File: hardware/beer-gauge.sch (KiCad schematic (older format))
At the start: 32 parts, among them J1 OLED_MODULE, P1 CONN_01X04, P2 CONN_01X04, P3 CONN_01X04, P4 CONN_01X04, U1 ADS1232IPW, U5 TCA9543A, U6 SN74LVC1G58

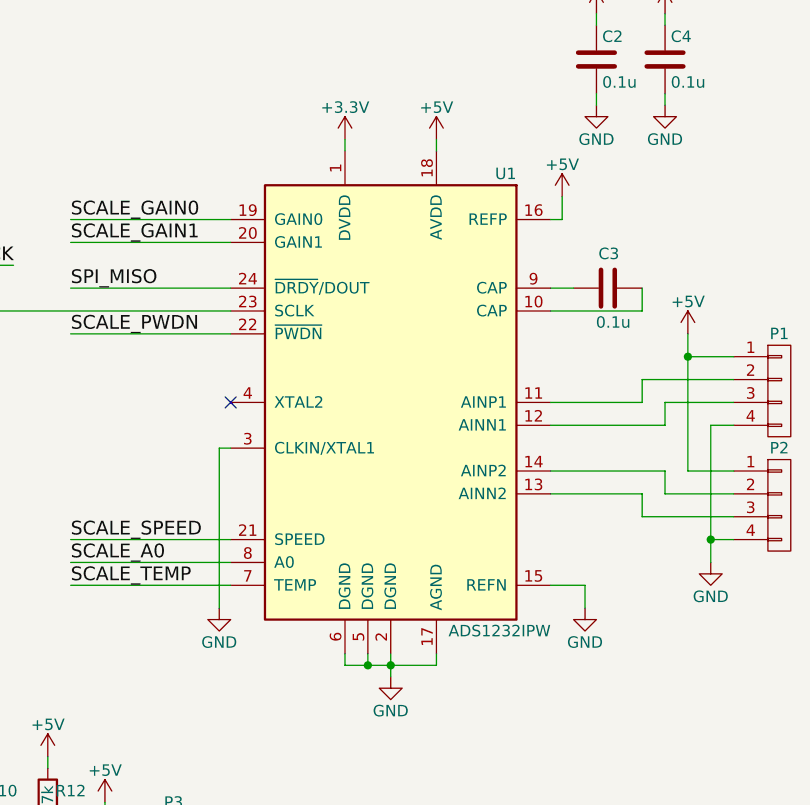
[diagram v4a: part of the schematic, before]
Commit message: Updating layout with schematic changes
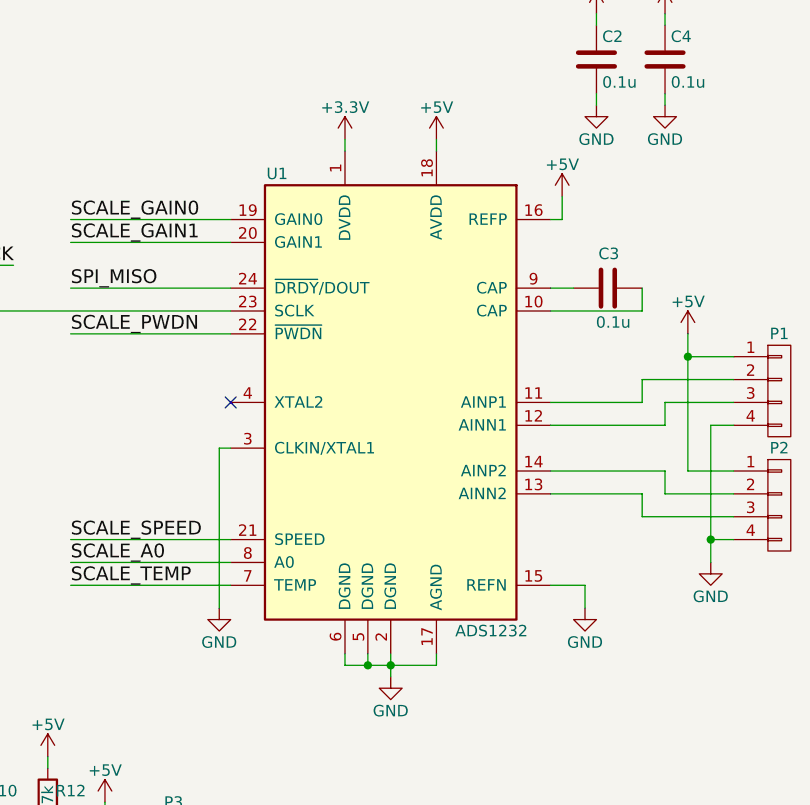
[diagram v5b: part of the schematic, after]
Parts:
- U1: value ADS1232IPW -> ADS1232
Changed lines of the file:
@@
 U 1 1 577FD904
 P 8100 2750
-F 0 "U1" H 7550 3750 50  0000 L CNN
-F 1 "ADS1232IPW" H 7400 1750 50  0000 L CNN
+F 0 "U1" H 8550 3750 50  0000 L CNN
+F 1 "ADS1232" H 7500 1750 50  0000 L CNN
 F 2 "Housings_SSOP:TSSOP-24_4.4x7.8mm_Pitch0.65mm" H 8100 2750 50  0001 C CIN
 F 3 "" H 8100 2750 50  0000 C CNN

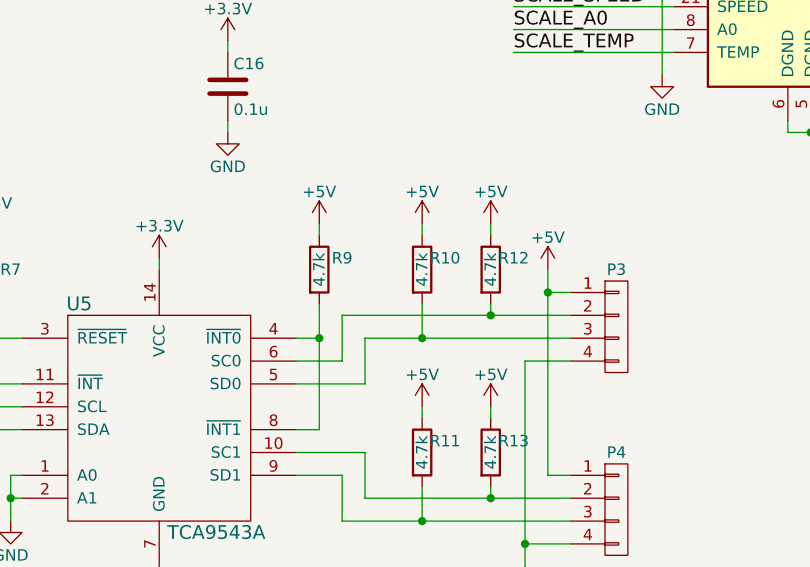
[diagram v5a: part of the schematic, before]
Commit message: Finished layout of traces
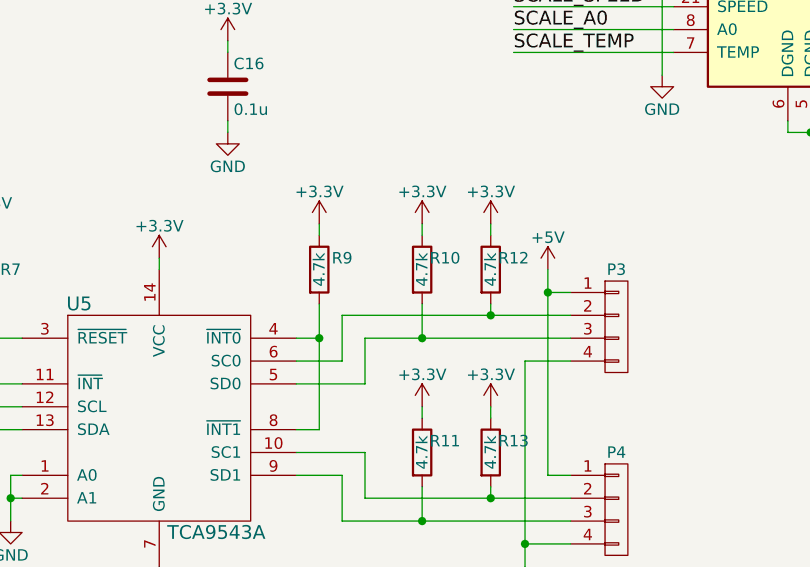
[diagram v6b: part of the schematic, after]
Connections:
- net +3V3: now also R10.1, R11.1, R12.1, R13.1, R9.1
- net +5V: no longer R10.1, R11.1, R12.1, R13.1, R9.1
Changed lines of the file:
@@
 	5750 4800 5850 4800
 Connection ~ 5850 4800
-$Comp
-L +5V #PWR033
-U 1 1 578242EC
-P 5850 4300
-F 0 "#PWR033" H 5850 4150 50  0001 C CNN
-F 1 "+5V" H 5850 4440 50  0000 C CNN
-F 2 "" H 5850 4300 50  0000 C CNN
-F 3 "" H 5850 4300 50  0000 C CNN
-	1    5850 4300
-	1    0    0    -1
-$EndComp
 Wire Wire Line
 	5850 4300 5850 4350
@@
 	6300 5450 6300 5600
 Connection ~ 6300 5600
-$Comp
-L +5V #PWR034
-U 1 1 57824D40
-P 6300 4300
-F 0 "#PWR034" H 6300 4150 50  0001 C CNN
-F 1 "+5V" H 6300 4440 50  0000 C CNN
-F 2 "" H 6300 4300 50  0000 C CNN
-F 3 "" H 6300 4300 50  0000 C CNN
-	1    6300 4300
-	1    0    0    -1
-$EndComp
-$Comp
-L +5V #PWR035
-U 1 1 57824E9B
-P 6600 4300
-F 0 "#PWR035" H 6600 4150 50  0001 C CNN
-F 1 "+5V" H 6600 4440 50  0000 C CNN
-F 2 "" H 6600 4300 50  0000 C CNN
-F 3 "" H 6600 4300 50  0000 C CNN
-	1    6600 4300
-	1    0    0    -1
-$EndComp
-$Comp
-L +5V #PWR036
-U 1 1 57824FF6
-P 6300 5100
-F 0 "#PWR036" H 6300 4950 50  0001 C CNN
-F 1 "+5V" H 6300 5240 50  0000 C CNN
-F 2 "" H 6300 5100 50  0000 C CNN
-F 3 "" H 6300 5100 50  0000 C CNN
-	1    6300 5100
-	1    0    0    -1
-$EndComp
-$Comp
-L +5V #PWR037
-U 1 1 57825151
-P 6600 5100
-F 0 "#PWR037" H 6600 4950 50  0001 C CNN
-F 1 "+5V" H 6600 5240 50  0000 C CNN
-F 2 "" H 6600 5100 50  0000 C CNN
-F 3 "" H 6600 5100 50  0000 C CNN
-	1    6600 5100
-	1    0    0    -1
-$EndComp
 Wire Wire Line
 	6600 5100 6600 5150
@@
 Wire Wire Line
 	6600 4300 6600 4350
+$Comp
+L +3.3V #PWR?
+U 1 1 577D9D9F
+P 5850 4300
+F 0 "#PWR?" H 5850 4150 50  0001 C CNN
+F 1 "+3.3V" H 5850 4440 50  0000 C CNN
+F 2 "" H 5850 4300 50  0000 C CNN
+F 3 "" H 5850 4300 50  0000 C CNN
+	1    5850 4300
+	1    0    0    -1
+$EndComp
+$Comp
+L +3.3V #PWR?
+U 1 1 577D9EFA
+P 6300 4300
+F 0 "#PWR?" H 6300 4150 50  0001 C CNN
+F 1 "+3.3V" H 6300 4440 50  0000 C CNN
+F 2 "" H 6300 4300 50  0000 C CNN
+F 3 "" H 6300 4300 50  0000 C CNN
+	1    6300 4300
+	1    0    0    -1
+$EndComp
+$Comp
+L +3.3V #PWR?
+U 1 1 577DA055
+P 6600 4300
+F 0 "#PWR?" H 6600 4150 50  0001 C CNN
+F 1 "+3.3V" H 6600 4440 50  0000 C CNN
+F 2 "" H 6600 4300 50  0000 C CNN
+F 3 "" H 6600 4300 50  0000 C CNN
+	1    6600 4300
+	1    0    0    -1
+$EndComp
+$Comp
+L +3.3V #PWR?
+U 1 1 577DA711
+P 6300 5100
+F 0 "#PWR?" H 6300 4950 50  0001 C CNN
+F 1 "+3.3V" H 6300 5240 50  0000 C CNN
+F 2 "" H 6300 5100 50  0000 C CNN
+F 3 "" H 6300 5100 50  0000 C CNN
+	1    6300 5100
+	1    0    0    -1
+$EndComp
+$Comp
+L +3.3V #PWR?
+U 1 1 577DA86C
+P 6600 5100
+F 0 "#PWR?" H 6600 4950 50  0001 C CNN
+F 1 "+3.3V" H 6600 5240 50  0000 C CNN
+F 2 "" H 6600 5100 50  0000 C CNN
+F 3 "" H 6600 5100 50  0000 C CNN
+	1    6600 5100
+	1    0    0    -1
+$EndComp
 $EndSCHEMATC

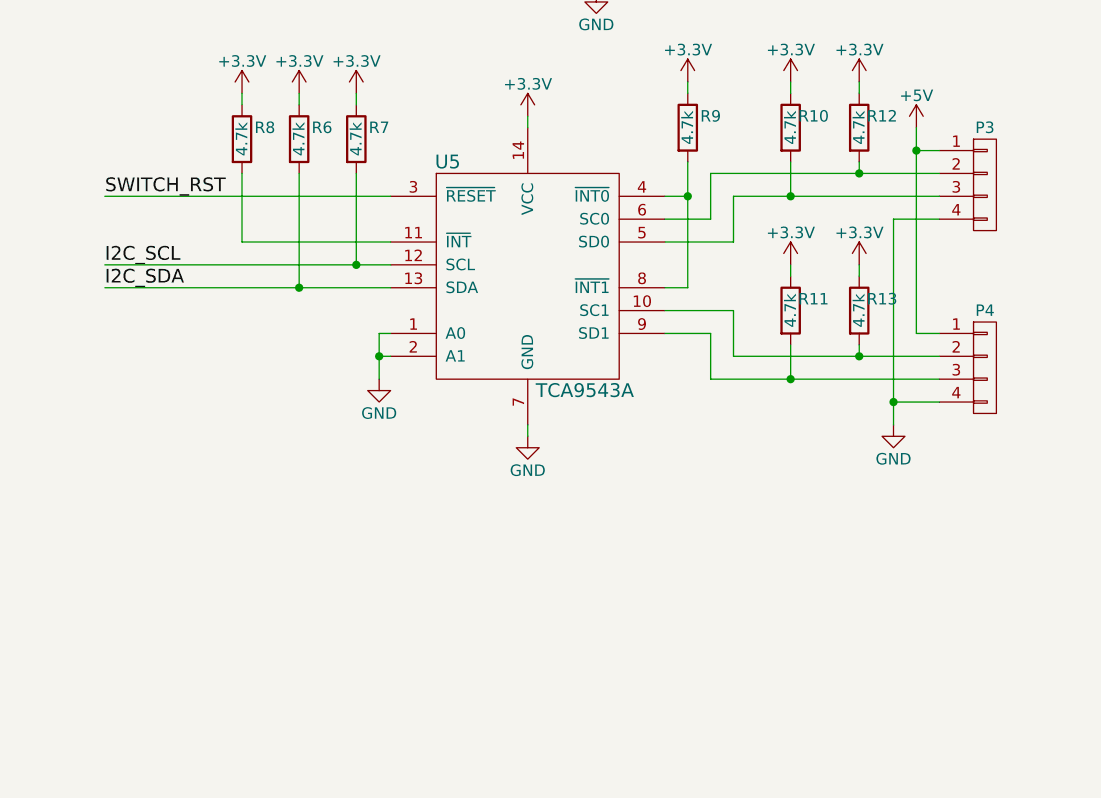
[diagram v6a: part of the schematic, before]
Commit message: Added DC jack for 5V input.  Updated layout
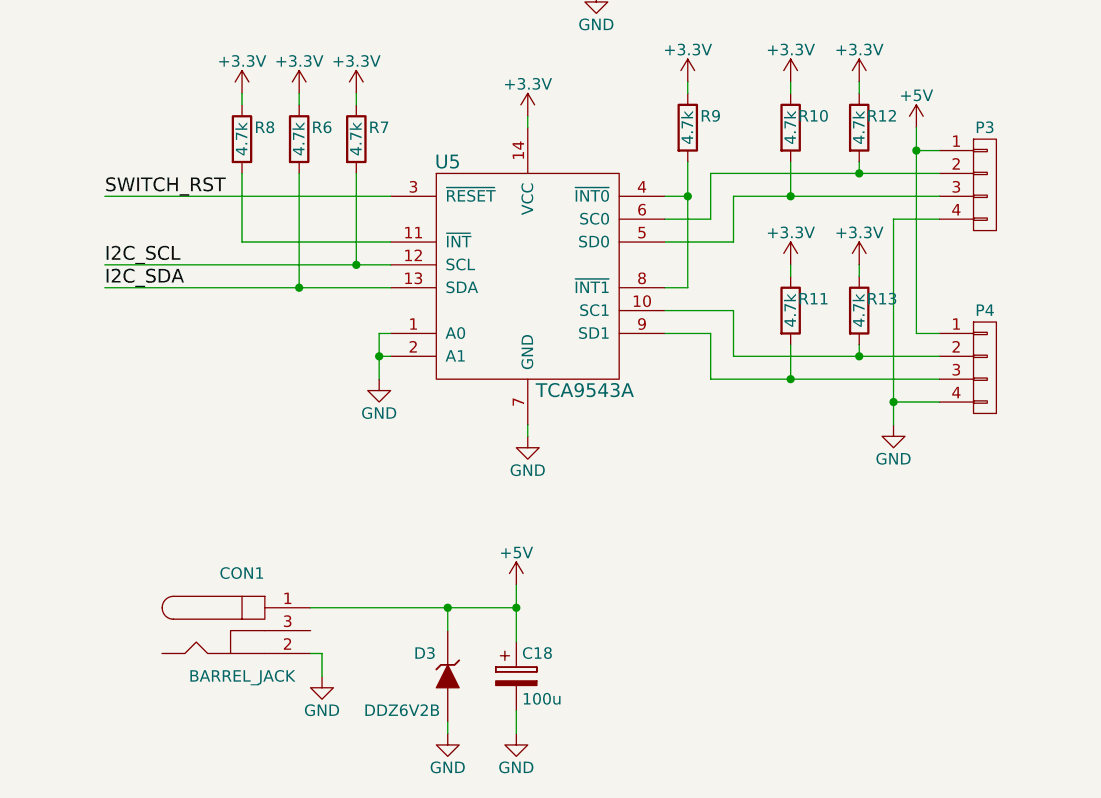
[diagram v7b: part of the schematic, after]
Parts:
- added C18: 100u, Capacitors_Tantalum_SMD:TantalC_SizeD_EIA-7343_Reflow, symbol CP
- added CON1: BARREL_JACK, footprint:PJ-070AH-SMT, symbol BARREL_JACK
- added D3: DDZ6V2B, Diodes_SMD:SOD-123, symbol ZENER
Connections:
- net +5V: now also C18.1, CON1.1, D3.1 (K)
- net GND: now also C18.2, CON1.2, D3.2 (A)
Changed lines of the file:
@@
 	6850 4500 6850 5400
 Wire Wire Line
-	6950 4800 6050 4800
+	6050 4800 6950 4800
 Wire Wire Line
 	6050 4800 6050 5000
@@
 	6050 5000 5750 5000
 Wire Wire Line
-	6950 4700 5950 4700
+	5950 4700 6950 4700
 Wire Wire Line
 	5950 4700 5950 4900
@@
 Connection ~ 6750 5700
 Wire Wire Line
-	6950 5500 6050 5500
+	6050 5500 6950 5500
 Wire Wire Line
 	6050 5500 6050 5300
@@
 	6050 5300 5750 5300
 Wire Wire Line
-	6950 5600 5950 5600
+	5950 5600 6950 5600
 Wire Wire Line
 	5950 5600 5950 5400
@@
 $EndComp
 Wire Wire Line
-	5750 5200 5850 5200
-Wire Wire Line
-	5850 5200 5850 4650
+	5850 5200 5750 5200
+Wire Wire Line
+	5850 4650 5850 5200
 Wire Wire Line
 	5750 4800 5850 4800
@@
 	6600 4300 6600 4350
 $Comp
-L +3.3V #PWR?
+L +3.3V #PWR033
 U 1 1 577D9D9F
 P 5850 4300
-F 0 "#PWR?" H 5850 4150 50  0001 C CNN
+F 0 "#PWR033" H 5850 4150 50  0001 C CNN
 F 1 "+3.3V" H 5850 4440 50  0000 C CNN
 F 2 "" H 5850 4300 50  0000 C CNN
@@
 $EndComp
 $Comp
-L +3.3V #PWR?
+L +3.3V #PWR034
 U 1 1 577D9EFA
 P 6300 4300
-F 0 "#PWR?" H 6300 4150 50  0001 C CNN
+F 0 "#PWR034" H 6300 4150 50  0001 C CNN
 F 1 "+3.3V" H 6300 4440 50  0000 C CNN
 F 2 "" H 6300 4300 50  0000 C CNN
@@
 $EndComp
 $Comp
-L +3.3V #PWR?
+L +3.3V #PWR035
 U 1 1 577DA055
 P 6600 4300
-F 0 "#PWR?" H 6600 4150 50  0001 C CNN
+F 0 "#PWR035" H 6600 4150 50  0001 C CNN
 F 1 "+3.3V" H 6600 4440 50  0000 C CNN
 F 2 "" H 6600 4300 50  0000 C CNN
@@
 $EndComp
 $Comp
-L +3.3V #PWR?
+L +3.3V #PWR036
 U 1 1 577DA711
 P 6300 5100
-F 0 "#PWR?" H 6300 4950 50  0001 C CNN
+F 0 "#PWR036" H 6300 4950 50  0001 C CNN
 F 1 "+3.3V" H 6300 5240 50  0000 C CNN
 F 2 "" H 6300 5100 50  0000 C CNN
@@
 $EndComp
 $Comp
-L +3.3V #PWR?
+L +3.3V #PWR037
 U 1 1 577DA86C
 P 6600 5100
-F 0 "#PWR?" H 6600 4950 50  0001 C CNN
+F 0 "#PWR037" H 6600 4950 50  0001 C CNN
 F 1 "+3.3V" H 6600 5240 50  0000 C CNN
 F 2 "" H 6600 5100 50  0000 C CNN
@@
 	1    0    0    -1
 $EndComp
+$Comp
+L ZENER D3
+U 1 1 577EF42F
+P 4800 6900
+F 0 "D3" V 4700 6800 50  0000 C CNN
+F 1 "DDZ6V2B" V 4950 6700 50  0000 C CNN
+F 2 "Diodes_SMD:SOD-123" H 4800 6900 50  0001 C CNN
+F 3 "" H 4800 6900 50  0000 C CNN
+	1    4800 6900
+	0    1    1    0
+$EndComp
+$Comp
+L GND #PWR038
+U 1 1 577F0116
+P 4800 7150
+F 0 "#PWR038" H 4800 6900 50  0001 C CNN
+F 1 "GND" H 4800 7000 50  0000 C CNN
+F 2 "" H 4800 7150 50  0000 C CNN
+F 3 "" H 4800 7150 50  0000 C CNN
+	1    4800 7150
+	1    0    0    -1
+$EndComp
+$Comp
+L CP C18
+U 1 1 577F0255
+P 5100 6900
+F 0 "C18" H 5125 7000 50  0000 L CNN
+F 1 "100u" H 5125 6800 50  0000 L CNN
+F 2 "Capacitors_Tantalum_SMD:TantalC_SizeD_EIA-7343_Reflow" H 5138 6750 50  0001 C CNN
+F 3 "" H 5100 6900 50  0000 C CNN
+	1    5100 6900
+	1    0    0    -1
+$EndComp
+$Comp
+L GND #PWR039
+U 1 1 577F0F27
+P 5100 7150
+F 0 "#PWR039" H 5100 6900 50  0001 C CNN
+F 1 "GND" H 5100 7000 50  0000 C CNN
+F 2 "" H 5100 7150 50  0000 C CNN
+F 3 "" H 5100 7150 50  0000 C CNN
+	1    5100 7150
+	1    0    0    -1
+$EndComp
+$Comp
+L BARREL_JACK CON1
+U 1 1 577F14E8
+P 3900 6700
+F 0 "CON1" H 3900 6950 50  0000 C CNN
+F 1 "BARREL_JACK" H 3900 6500 50  0000 C CNN
+F 2 "footprint:PJ-070AH-SMT" H 3900 6700 50  0001 C CNN
+F 3 "" H 3900 6700 50  0000 C CNN
+	1    3900 6700
+	1    0    0    -1
+$EndComp
+$Comp
+L GND #PWR040
+U 1 1 577F1672
+P 4250 6900
+F 0 "#PWR040" H 4250 6650 50  0001 C CNN
+F 1 "GND" H 4250 6750 50  0000 C CNN
+F 2 "" H 4250 6900 50  0000 C CNN
+F 3 "" H 4250 6900 50  0000 C CNN
+	1    4250 6900
+	1    0    0    -1
+$EndComp
+Wire Wire Line
+	4200 6800 4250 6800
+Wire Wire Line
+	4250 6800 4250 6900
+Wire Wire Line
+	4200 6600 5100 6600
+Wire Wire Line
+	4800 6600 4800 6700
+Wire Wire Line
+	4800 7150 4800 7100
+Wire Wire Line
+	5100 7150 5100 7050
+Wire Wire Line
+	5100 6500 5100 6750
+Connection ~ 4800 6600
+$Comp
+L +5V #PWR041
+U 1 1 577F2888
+P 5100 6500
+F 0 "#PWR041" H 5100 6350 50  0001 C CNN
+F 1 "+5V" H 5100 6640 50  0000 C CNN
+F 2 "" H 5100 6500 50  0000 C CNN
+F 3 "" H 5100 6500 50  0000 C CNN
+	1    5100 6500
+	1    0    0    -1
+$EndComp
+Connection ~ 5100 6600
 $EndSCHEMATC

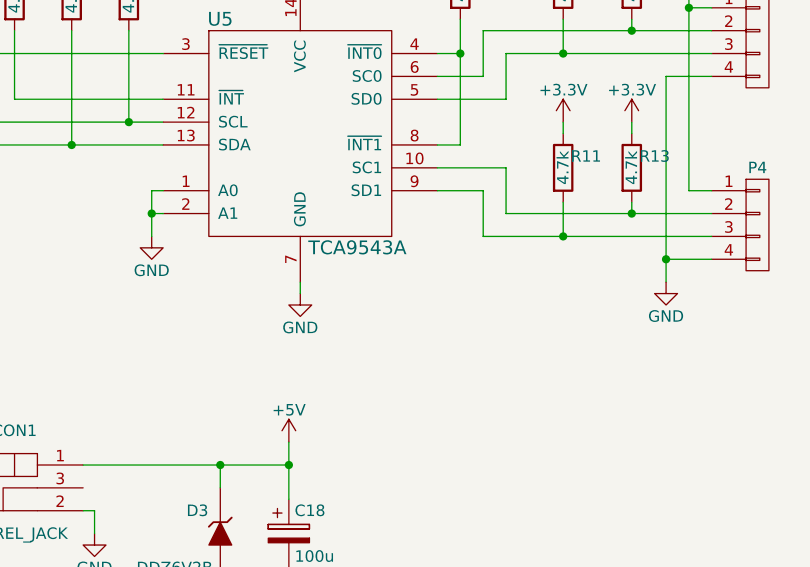
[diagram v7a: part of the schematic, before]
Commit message: Created kicad project and schematic for I2C sensor board
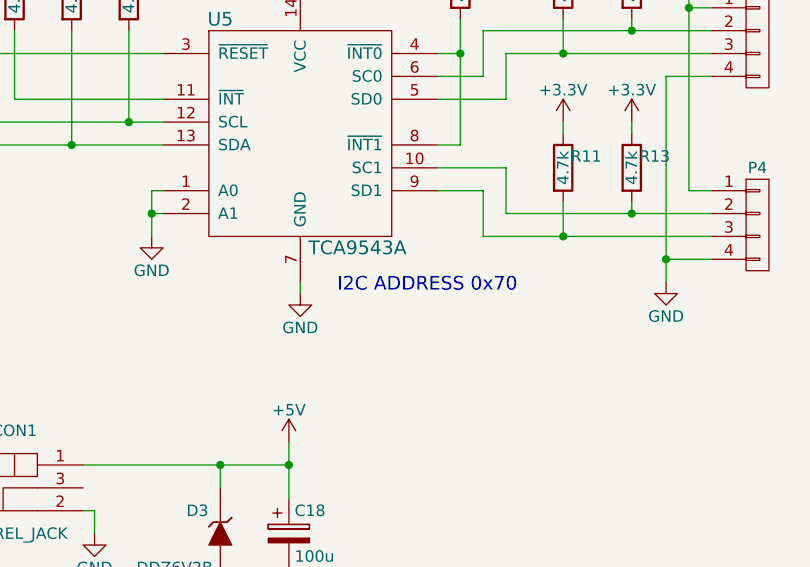
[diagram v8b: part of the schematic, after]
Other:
- note added: "I2C ADDRESS 0x70"
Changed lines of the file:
@@
 $EndComp
 Connection ~ 5100 6600
+Text Notes 6100 5850 2    60   ~ 0
+I2C ADDRESS 0x70
 $EndSCHEMATC
